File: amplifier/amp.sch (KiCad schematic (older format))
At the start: 6 parts, among them P1 PWR, U1 OPAMP

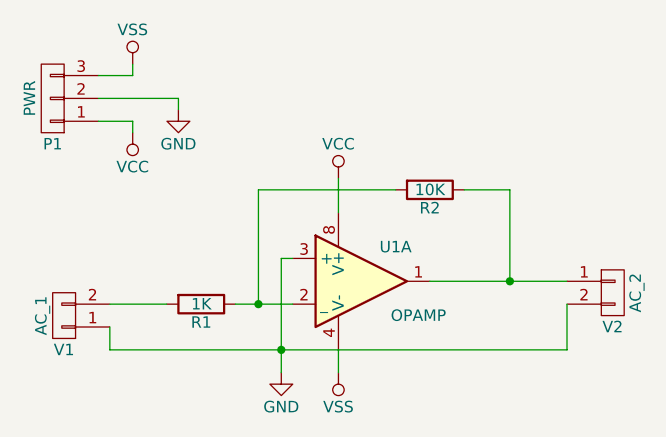
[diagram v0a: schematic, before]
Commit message: Added Simulation Circuits and POV board
Added a BJT characteristics simulation circuit
Add a Voltage Divider simulation circuit
Add an amplifier simulation circuit
Add a Nokia LCD breakout board
Add a POV LED MKL05Z board
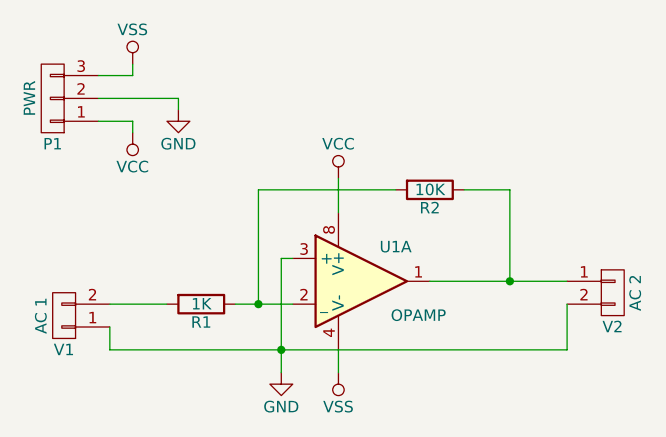
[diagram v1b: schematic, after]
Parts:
- V1: value AC_1 -> AC 1
- V2: value AC_2 -> AC 2
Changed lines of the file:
@@
 LIBS:contrib
 LIBS:valves
+LIBS:amp-cache
 EELAYER 25 0
 EELAYER END
@@
 P 4150 3650
 F 0 "V1" H 4150 3800 50  0000 C CNN
-F 1 "AC_1" V 4250 3650 50  0000 C CNN
+F 1 "AC 1" V 4250 3650 50  0000 C CNN
 F 2 "" H 4150 3650 50  0000 C CNN
 F 3 "" H 4150 3650 50  0000 C CNN
@@
 P 6550 3550
 F 0 "V2" H 6550 3400 50  0000 C CNN
-F 1 "AC_2" V 6650 3550 50  0000 C CNN
+F 1 "AC 2" V 6650 3550 50  0000 C CNN
 F 2 "" H 6550 3550 50  0000 C CNN
 F 3 "" H 6550 3550 50  0000 C CNN
